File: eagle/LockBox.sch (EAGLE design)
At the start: 8 parts

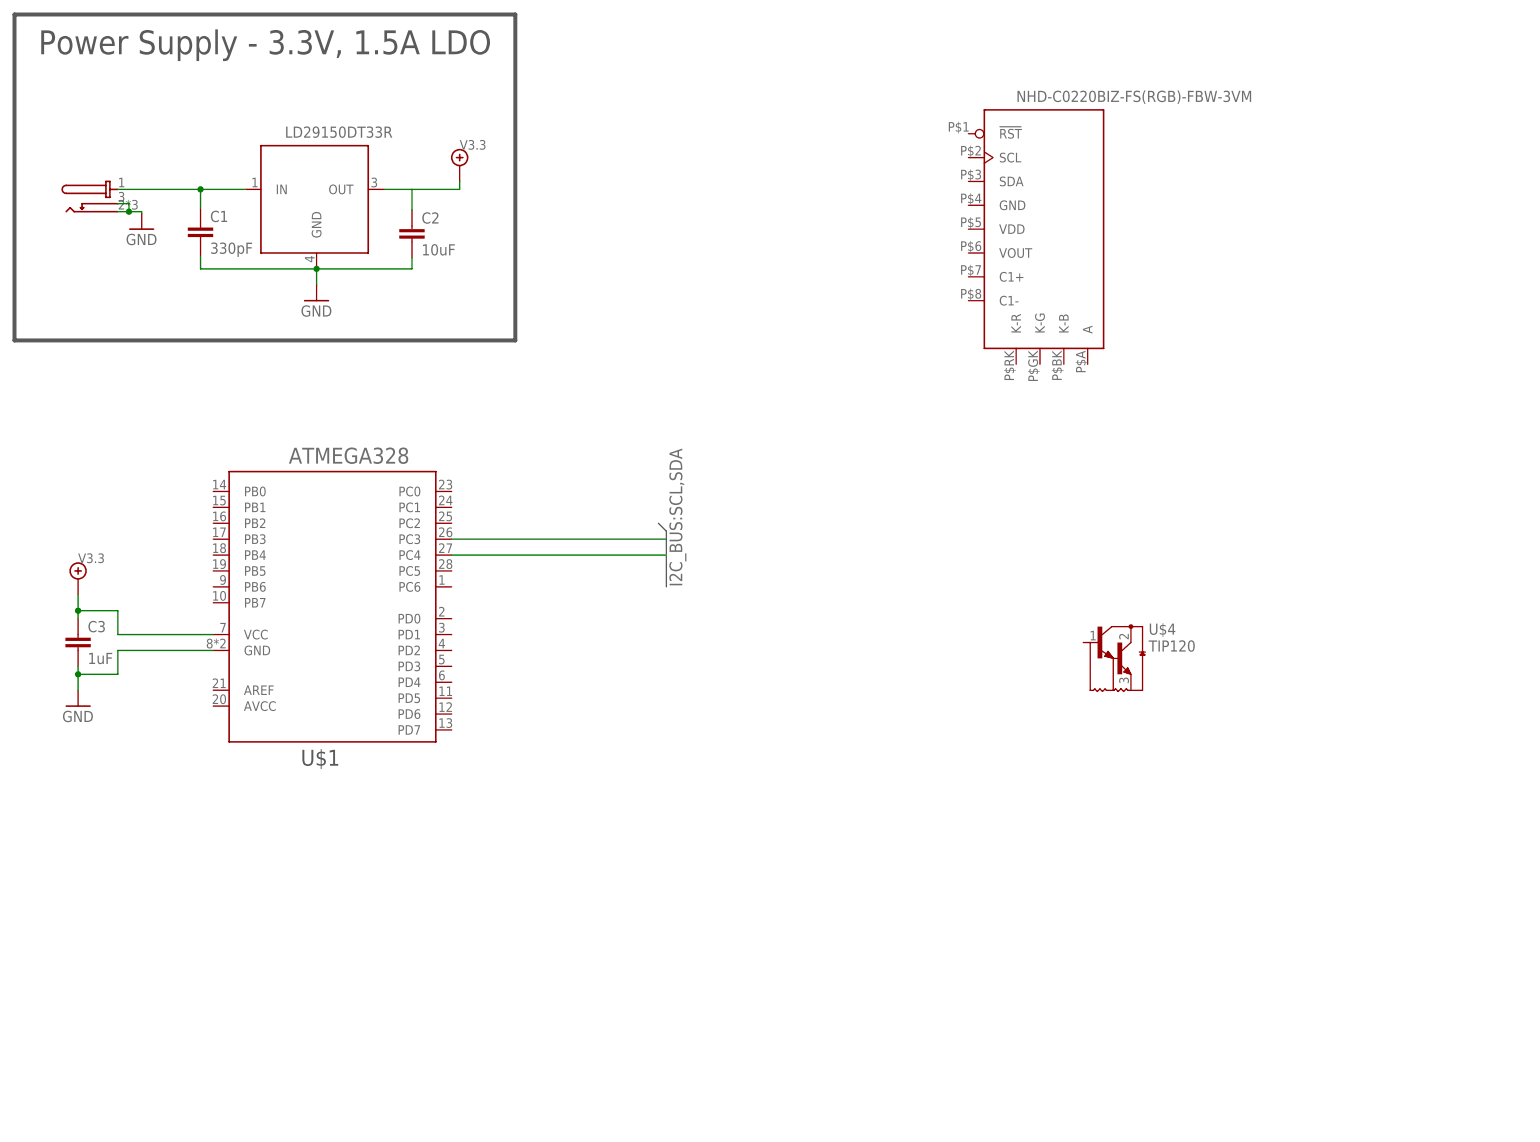
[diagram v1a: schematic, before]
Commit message: Added I2C bus and pull up resistors to the LCD screen.
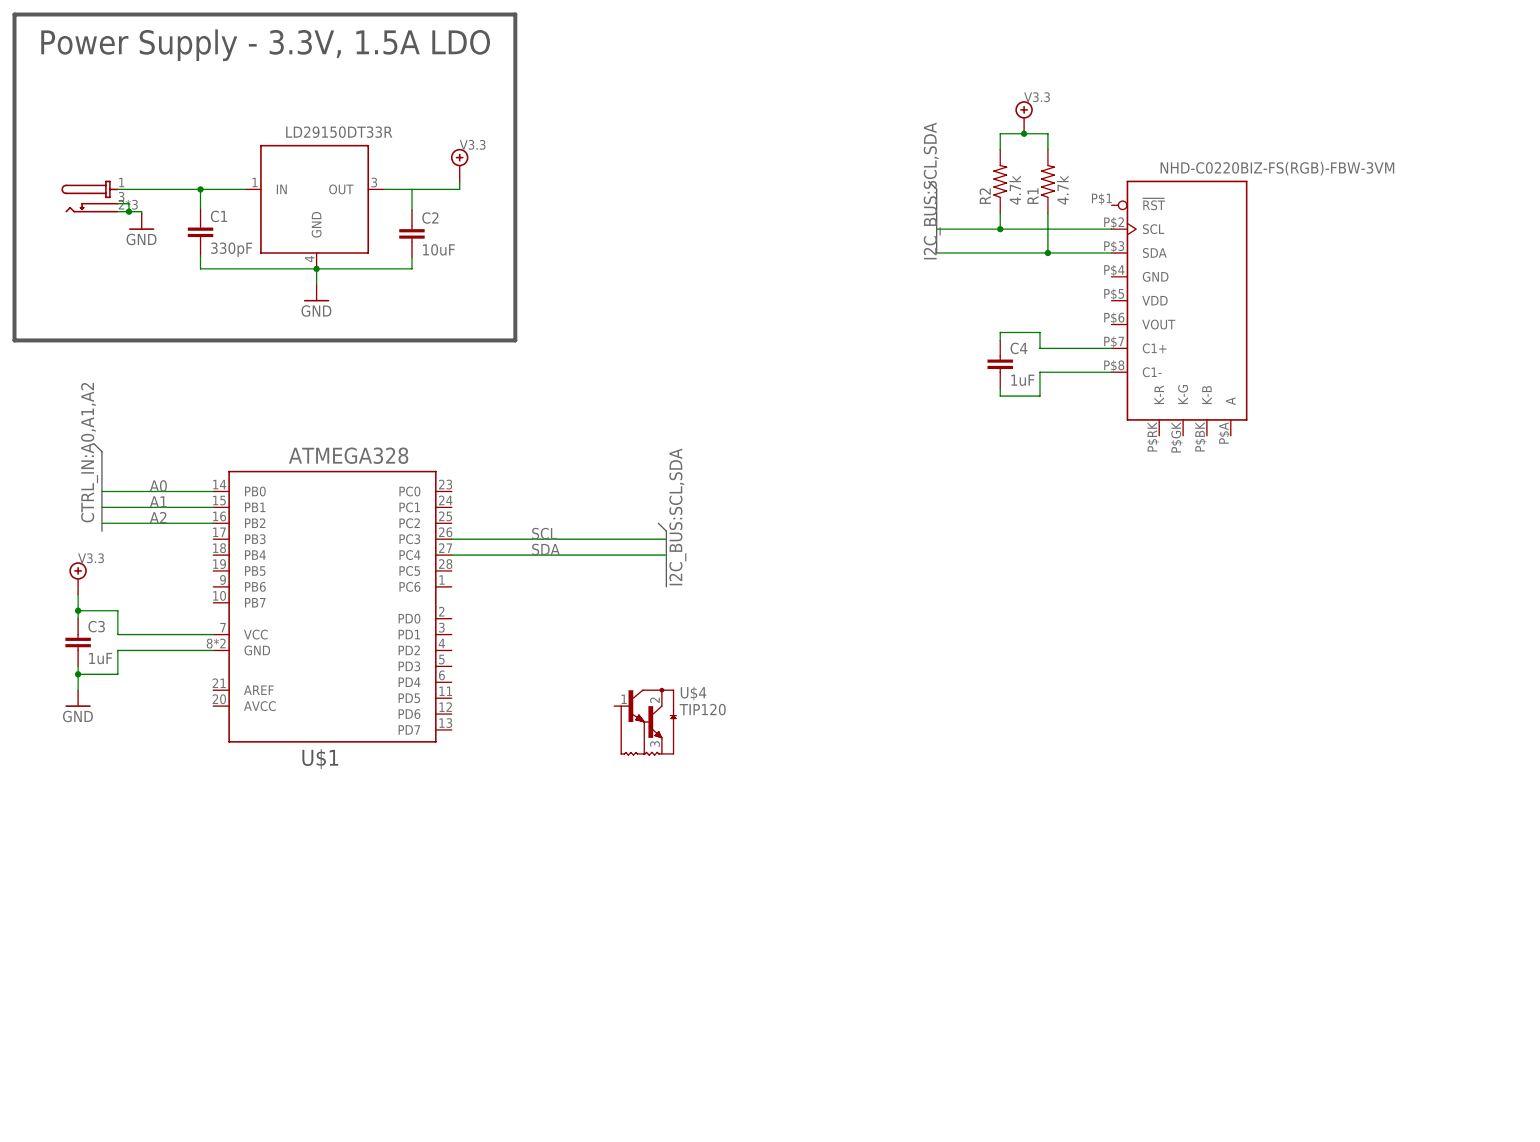
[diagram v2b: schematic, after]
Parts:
- added C4: 1uF, LockBox:C
- added R1, R2: 4.7k, LockBox:R-US_M0805
- U$1: PB0 (none) -> GPIO; PB1 (none) -> GPIO; PB2 (none) -> GPIO
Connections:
- new net A0: U$1.PB0
- new net A1: U$1.PB1
- new net A2: U$1.PB2
- new net N$2: C4.1, U$5.C1+
- new net N$3: C4.2, U$5.C1-
- net P$1: now also R1.2, R2.2
- net SCL: now also R2.1, U$5.SCL
- net SDA: now also R1.1, U$5.SDA
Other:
- moved on the sheet: U$4
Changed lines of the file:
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@@
 <part name="V1" library="LockBox" deviceset="V3.3" device=""/>
 <part name="U$1" library="LockBox" deviceset="ATMEGA328" device="">
+<attribute name="PB0" value="GPIO"/>
+<attribute name="PB1" value="GPIO"/>
+<attribute name="PB2" value="GPIO"/>
 <attribute name="PC3" value="SCL"/>
 <attribute name="PC4" value="SDA"/>
@@
 <part name="GND3" library="LockBox" deviceset="GND" device=""/>
 <part name="V2" library="LockBox" deviceset="V3.3" device=""/>
+<part name="C4" library="LockBox" deviceset="C" device="" value="1uF"/>
+<part name="R1" library="LockBox" deviceset="R-US_" device="M0805" value="4.7k"/>
+<part name="R2" library="LockBox" deviceset="R-US_" device="M0805" value="4.7k"/>
+<part name="V3" library="LockBox" deviceset="V3.3" device=""/>
 </parts>
 <sheets>
@@
 <instance part="U$2" gate="G$1" x="55.88" y="151.13"/>
 <instance part="U$3" gate="G$1" x="26.035" y="151.765"/>
-<instance part="U$4" gate="G$1" x="187.96" y="77.47"/>
-<instance part="U$5" gate="G$1" x="176.53" y="147.32"/>
+<instance part="U$4" gate="G$1" x="113.03" y="67.31"/>
+<instance part="U$5" gate="G$1" x="199.39" y="135.89"/>
 <instance part="C1" gate="G$1" x="41.148" y="146.812"/>
 <instance part="C2" gate="G$1" x="74.93" y="146.558"/>
@@
 <attribute name="PC3" x="62.23" y="88.265" size="1.778" layer="96" display="off"/>
 <attribute name="PC4" x="62.23" y="88.265" size="1.778" layer="96" display="off"/>
+<attribute name="PB0" x="62.23" y="88.265" size="2.032" layer="96" display="off"/>
+<attribute name="PB1" x="62.23" y="88.265" size="2.032" layer="96" display="off"/>
+<attribute name="PB2" x="62.23" y="88.265" size="2.032" layer="96" display="off"/>
 </instance>
 <instance part="C3" gate="G$1" x="21.59" y="81.28"/>
 <instance part="GND3" gate="1" x="21.59" y="69.85"/>
 <instance part="V2" gate="G1" x="21.59" y="90.17"/>
+<instance part="C4" gate="G$1" x="168.91" y="125.73"/>
+<instance part="R1" gate="G$1" x="176.53" y="153.67" rot="R90"/>
+<instance part="R2" gate="G$1" x="168.91" y="153.67" rot="R90"/>
+<instance part="V3" gate="G1" x="172.72" y="163.83"/>
 </instances>
 <busses>
@@
 <wire x1="115.57" y1="97.79" x2="115.57" y2="88.9" width="0.762" layer="92"/>
 <label x="118.11" y="88.9" size="2.032" layer="95" rot="R90"/>
+</segment>
+<segment>
+<wire x1="157.48" y1="153.67" x2="158.75" y2="152.4" width="0.762" layer="92"/>
+<wire x1="158.75" y1="152.4" x2="158.75" y2="142.24" width="0.762" layer="92"/>
+<label x="158.75" y="140.97" size="2.032" layer="95" rot="R90"/>
+</segment>
+</bus>
+<bus name="CTRL_IN:A0,A1,A2">
+<segment>
+<wire x1="24.13" y1="111.76" x2="25.4" y2="110.49" width="0.762" layer="92"/>
+<wire x1="25.4" y1="110.49" x2="25.4" y2="97.79" width="0.762" layer="92"/>
+<label x="24.13" y="99.06" size="2.032" layer="95" rot="R90"/>
 </segment>
 </bus>
@@
 <junction x="21.59" y="85.09"/>
 </segment>
+<segment>
+<pinref part="R2" gate="G$1" pin="2"/>
+<wire x1="168.91" y1="158.75" x2="168.91" y2="161.29" width="0.1524" layer="91"/>
+<wire x1="168.91" y1="161.29" x2="172.72" y2="161.29" width="0.1524" layer="91"/>
+<pinref part="R1" gate="G$1" pin="2"/>
+<wire x1="172.72" y1="161.29" x2="176.53" y2="161.29" width="0.1524" layer="91"/>
+<wire x1="176.53" y1="161.29" x2="176.53" y2="158.75" width="0.1524" layer="91"/>
+<pinref part="V3" gate="G1" pin="P$1"/>
+<junction x="172.72" y="161.29"/>
+</segment>
 </net>
 <net name="SCL" class="0">
@@
 <pinref part="U$1" gate="G$1" pin="PC3"/>
 <wire x1="115.57" y1="96.52" x2="81.28" y2="96.52" width="0.1524" layer="91"/>
+<label x="93.98" y="96.52" size="1.778" layer="95"/>
+</segment>
+<segment>
+<pinref part="U$5" gate="G$1" pin="SCL"/>
+<wire x1="158.75" y1="146.05" x2="168.91" y2="146.05" width="0.1524" layer="91"/>
+<pinref part="R2" gate="G$1" pin="1"/>
+<wire x1="168.91" y1="146.05" x2="186.69" y2="146.05" width="0.1524" layer="91"/>
+<wire x1="168.91" y1="146.05" x2="168.91" y2="148.59" width="0.1524" layer="91"/>
+<junction x="168.91" y="146.05"/>
 </segment>
 </net>
@@
 <pinref part="U$1" gate="G$1" pin="PC4"/>
 <wire x1="115.57" y1="93.98" x2="81.28" y2="93.98" width="0.1524" layer="91"/>
-</segment>
-</net>
+<label x="93.98" y="93.98" size="1.778" layer="95"/>
+</segment>
+<segment>
+<pinref part="U$5" gate="G$1" pin="SDA"/>
+<wire x1="158.75" y1="142.24" x2="176.53" y2="142.24" width="0.1524" layer="91"/>
+<pinref part="R1" gate="G$1" pin="1"/>
+<wire x1="176.53" y1="142.24" x2="186.69" y2="142.24" width="0.1524" layer="91"/>
+<wire x1="176.53" y1="142.24" x2="176.53" y2="148.59" width="0.1524" layer="91"/>
+<junction x="176.53" y="142.24"/>
+</segment>
+</net>
+<net name="A0" class="0">
+<segment>
+<pinref part="U$1" gate="G$1" pin="PB0"/>
+<wire x1="25.4" y1="104.14" x2="43.18" y2="104.14" width="0.1524" layer="91"/>
+<label x="33.02" y="104.14" size="1.778" layer="95"/>
+</segment>
+</net>
+<net name="A1" class="0">
+<segment>
+<pinref part="U$1" gate="G$1" pin="PB1"/>
+<wire x1="25.4" y1="101.6" x2="43.18" y2="101.6" width="0.1524" layer="91"/>
+<label x="33.02" y="101.6" size="1.778" layer="95"/>
+</segment>
+</net>
+<net name="A2" class="0">
+<segment>
+<pinref part="U$1" gate="G$1" pin="PB2"/>
+<wire x1="25.4" y1="99.06" x2="43.18" y2="99.06" width="0.1524" layer="91"/>
+<label x="33.02" y="99.06" size="1.778" layer="95"/>
+</segment>
+</net>
+<net name="N$2" class="0">
+<segment>
+<pinref part="U$5" gate="G$1" pin="C1+"/>
+<wire x1="186.69" y1="127" x2="175.26" y2="127" width="0.1524" layer="91"/>
+<wire x1="175.26" y1="127" x2="175.26" y2="129.54" width="0.1524" layer="91"/>
+<wire x1="175.26" y1="129.54" x2="168.91" y2="129.54" width="0.1524" layer="91"/>
+<pinref part="C4" gate="G$1" pin="1"/>
+<wire x1="168.91" y1="129.54" x2="168.91" y2="128.27" width="0.1524" layer="91"/>
+</segment>
+</net>
+<net name="N$3" class="0">
+<segment>
+<pinref part="U$5" gate="G$1" pin="C1-"/>
+<wire x1="186.69" y1="123.19" x2="175.26" y2="123.19" width="0.1524" layer="91"/>
+<wire x1="175.26" y1="123.19" x2="175.26" y2="119.38" width="0.1524" layer="91"/>
+<wire x1="175.26" y1="119.38" x2="168.91" y2="119.38" width="0.1524" layer="91"/>
+<pinref part="C4" gate="G$1" pin="2"/>
+<wire x1="168.91" y1="119.38" x2="168.91" y2="120.65" width="0.1524" layer="91"/>
+</segment>
+</net>
